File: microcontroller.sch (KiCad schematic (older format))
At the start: 8 parts

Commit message: Basic schematic with temparature and humidity sensor.
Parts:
- removed U?: STM32F072C8T, LQFP48, symbol STM32F072C8T
- added C?: 100n, symbol C
- added C?: C, symbol C
- added P?: DEBUG_UART, symbol CONN_01X03
- added R? (x2): 3k3, symbol R
- added SW?: SW_PUSH, symbol SW_PUSH
- added U?: STM32F072RB, symbol STM32F072RB
- added U?: HDC1080, symbol HDC1080
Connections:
- net labels added: CAN_RX, CAN_STANDBY, CAN_TX, GPIO_PB4_OUT, I2C1_SCL, I2C1_SDA, UART_RX, UART_TX
- wire segments 28 -> 63
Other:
- moved on the sheet: C?, X?

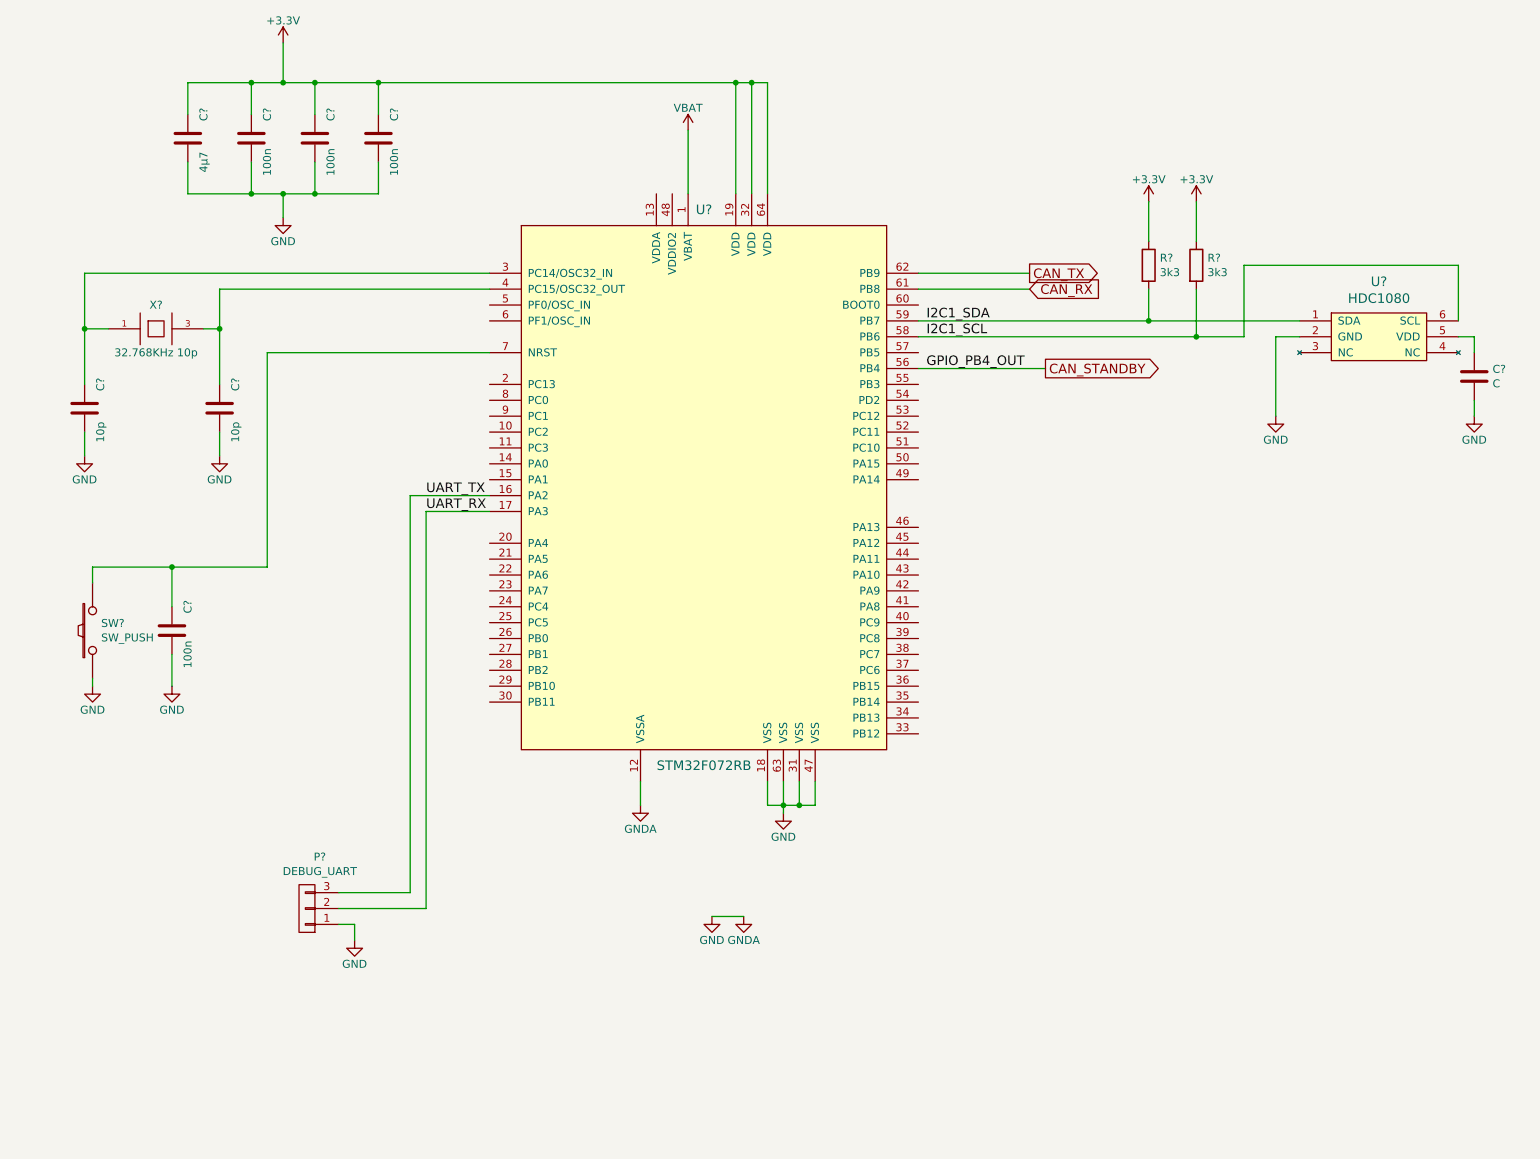
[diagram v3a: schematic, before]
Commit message: Add flash and debug connector.
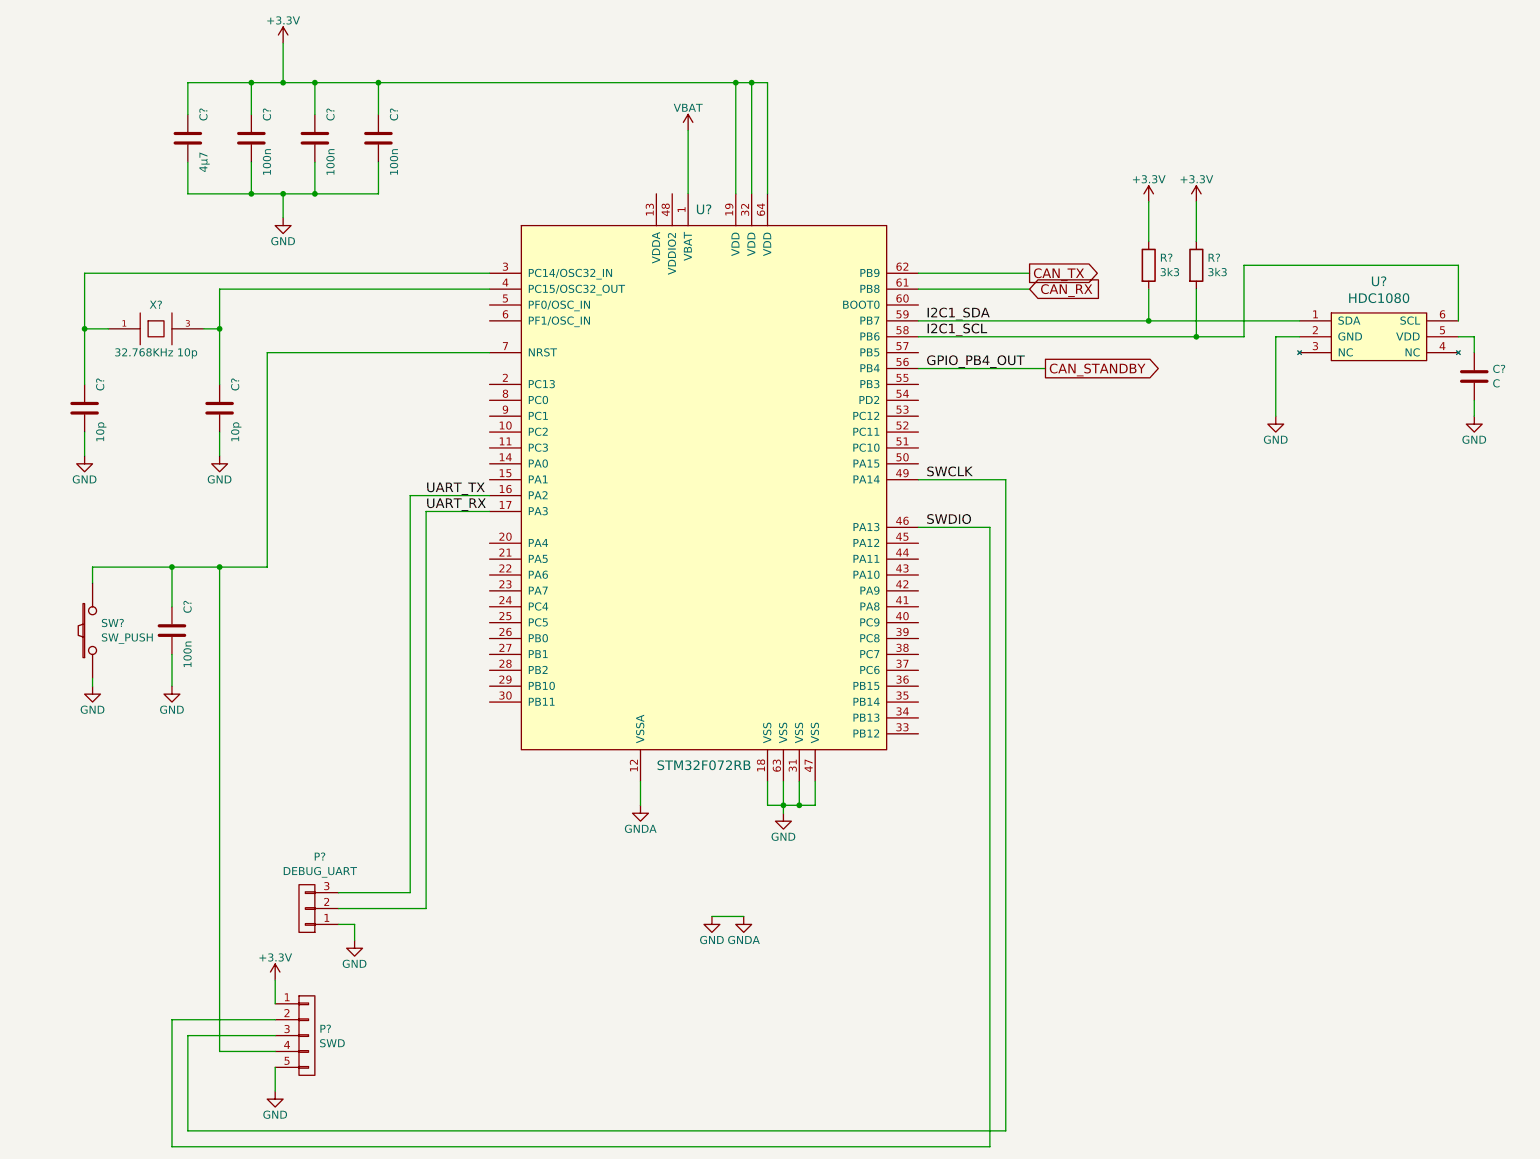
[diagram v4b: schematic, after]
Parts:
- added P?: SWD, symbol CONN_01X05
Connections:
- net +3V3: now also P?.1 (P1)
- net GND: now also P?.5 (P5)
- net SWDIO: now reaches U?.46 (PA13)
- net SWDIO: now also P?.2 (P2)
- net SWCLK: now reaches U?.49 (PA14)
- net SWCLK: now also P?.3 (P3)
- net at C?.1, SW?.2, U?.7 (NRST): now also P?.4 (P4)
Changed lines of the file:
@@
 Wire Wire Line
 	6200 2800 7000 2800
+$Comp
+L CONN_01X05 P?
+U 1 1 57AF82F1
+P 2350 7000
+F 0 "P?" H 2428 7041 50  0000 L CNN
+F 1 "SWD" H 2428 6950 50  0000 L CNN
+F 2 "" H 2350 7000 50  0000 C CNN
+F 3 "" H 2350 7000 50  0000 C CNN
+	1    2350 7000
+	1    0    0    -1
+$EndComp
+$Comp
+L GND #PWR?
+U 1 1 57AF8433
+P 2150 7350
+F 0 "#PWR?" H 2150 7100 50  0001 C CNN
+F 1 "GND" H 2150 7200 50  0000 C CNN
+F 2 "" H 2150 7350 60  0000 C CNN
+F 3 "" H 2150 7350 60  0000 C CNN
+	1    2150 7350
+	1    0    0    -1
+$EndComp
+Wire Wire Line
+	2150 7350 2150 7200
+$Comp
+L +3.3V #PWR?
+U 1 1 57AF8559
+P 2150 6650
+F 0 "#PWR?" H 2150 6500 50  0001 C CNN
+F 1 "+3.3V" H 2150 6790 50  0000 C CNN
+F 2 "" H 2150 6650 60  0000 C CNN
+F 3 "" H 2150 6650 60  0000 C CNN
+	1    2150 6650
+	1    0    0    -1
+$EndComp
+Wire Wire Line
+	2150 6800 2150 6650
+Wire Wire Line
+	2150 6900 1500 6900
+Text Label 6250 3800 0    60   ~ 0
+SWDIO
+Wire Wire Line
+	6200 3500 6750 3500
+Wire Wire Line
+	6750 3500 6750 7600
+Wire Wire Line
+	1600 7000 2150 7000
+Text Label 6250 3500 0    60   ~ 0
+SWCLK
+Wire Wire Line
+	1600 7000 1600 7600
+Wire Wire Line
+	1600 7600 6750 7600
+Wire Wire Line
+	6200 3800 6650 3800
+Wire Wire Line
+	6650 3800 6650 7700
+Wire Wire Line
+	6650 7700 1500 7700
+Wire Wire Line
+	1500 7700 1500 6900
+Wire Wire Line
+	2150 7100 1800 7100
+Wire Wire Line
+	1800 7100 1800 4050
+Connection ~ 1800 4050
 $EndSCHEMATC

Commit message: .
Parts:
- added Q?: Q_NMOS_DGS, symbol Q_NMOS_DGS
- C19, C20, C21: renamed from C?; footprint (none) -> Capacitors_SMD:C_0603_HandSoldering
- R15, R16: renamed from R?; footprint (none) -> Resistors_SMD:R_0603_HandSoldering
- U3: renamed from U?; footprint (none) -> can-node:LQFP64_STM
- gave numbers to parts that had none: 10
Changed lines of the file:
@@
 $EndDescr
 $Comp
-L +3.3V #PWR029
+L +3.3V #PWR028
 U 1 1 562B6336
 P 2200 750
-F 0 "#PWR029" H 2200 600 50  0001 C CNN
+F 0 "#PWR028" H 2200 600 50  0001 C CNN
 F 1 "+3.3V" H 2200 890 50  0000 C CNN
 F 2 "" H 2200 750 60  0000 C CNN
@@
 $EndComp
 $Comp
-L QUARTZCMS4 X?
+L QUARTZCMS4 X1
 U 1 1 562B633C
 P 1400 2550
-F 0 "X?" H 1400 2700 50  0000 C CNN
+F 0 "X1" H 1400 2700 50  0000 C CNN
 F 1 "32.768KHz 10p" H 1400 2400 50  0000 C CNN
-F 2 "" H 1400 2550 60  0000 C CNN
+F 2 "" H 1400 2550 60  0001 C CNN
 F 3 "" H 1400 2550 60  0000 C CNN
 	1    1400 2550
@@
 $EndComp
 $Comp
-L C C?
+L C C18
 U 1 1 562B6351
 P 1800 3050
-F 0 "C?" V 1900 3200 50  0000 C CNN
+F 0 "C18" V 1900 3200 50  0000 C CNN
 F 1 "10p" V 1900 2900 50  0000 C CNN
-F 2 "" H 1800 3050 60  0000 C CNN
+F 2 "" H 1800 3050 60  0001 C CNN
 F 3 "" H 1800 3050 60  0000 C CNN
 	1    1800 3050
@@
 $EndComp
 $Comp
-L C C?
+L C C15
 U 1 1 562B6358
 P 950 3050
-F 0 "C?" V 1050 3200 50  0000 C CNN
+F 0 "C15" V 1050 3200 50  0000 C CNN
 F 1 "10p" V 1050 2900 50  0000 C CNN
-F 2 "" H 950 3050 60  0000 C CNN
+F 2 "" H 950 3050 60  0001 C CNN
 F 3 "" H 950 3050 60  0000 C CNN
 	1    950  3050
@@
 $EndComp
 $Comp
-L GND #PWR030
+L GND #PWR029
 U 1 1 562B635F
 P 950 3350
-F 0 "#PWR030" H 950 3100 50  0001 C CNN
+F 0 "#PWR029" H 950 3100 50  0001 C CNN
 F 1 "GND" H 950 3200 50  0000 C CNN
 F 2 "" H 950 3350 60  0000 C CNN
@@
 $EndComp
 $Comp
-L GND #PWR031
+L GND #PWR030
 U 1 1 562B6365
 P 1800 3350
-F 0 "#PWR031" H 1800 3100 50  0001 C CNN
+F 0 "#PWR030" H 1800 3100 50  0001 C CNN
 F 1 "GND" H 1800 3200 50  0000 C CNN
 F 2 "" H 1800 3350 60  0000 C CNN
@@
 $EndComp
 $Comp
-L GND #PWR032
+L GND #PWR031
 U 1 1 562B636B
 P 5350 5600
-F 0 "#PWR032" H 5350 5350 50  0001 C CNN
+F 0 "#PWR031" H 5350 5350 50  0001 C CNN
 F 1 "GND" H 5350 5450 50  0000 C CNN
 F 2 "" H 5350 5600 60  0000 C CNN
@@
 $EndComp
 $Comp
-L GND #PWR033
+L GND #PWR032
 U 1 1 562B6371
 P 4900 6250
-F 0 "#PWR033" H 4900 6000 50  0001 C CNN
+F 0 "#PWR032" H 4900 6000 50  0001 C CNN
 F 1 "GND" H 4900 6100 50  0000 C CNN
 F 2 "" H 4900 6250 60  0000 C CNN
@@
 $EndComp
 $Comp
-L GNDA #PWR034
+L GNDA #PWR033
 U 1 1 562B6377
 P 4450 5550
-F 0 "#PWR034" H 4450 5300 50  0001 C CNN
+F 0 "#PWR033" H 4450 5300 50  0001 C CNN
 F 1 "GNDA" H 4450 5400 50  0000 C CNN
 F 2 "" H 4450 5550 60  0000 C CNN
@@
 $EndComp
 $Comp
-L GNDA #PWR035
+L GNDA #PWR034
 U 1 1 562B637D
 P 5100 6250
-F 0 "#PWR035" H 5100 6000 50  0001 C CNN
+F 0 "#PWR034" H 5100 6000 50  0001 C CNN
 F 1 "GNDA" H 5100 6100 50  0000 C CNN
 F 2 "" H 5100 6250 60  0000 C CNN
@@
 $EndComp
 $Comp
-L C C?
+L C C21
 U 1 1 562B6383
 P 2800 1350
-F 0 "C?" V 2900 1500 50  0000 C CNN
+F 0 "C21" V 2900 1500 50  0000 C CNN
 F 1 "100n" V 2900 1200 50  0000 C CNN
-F 2 "" H 2800 1350 60  0000 C CNN
+F 2 "Capacitors_SMD:C_0603_HandSoldering" H 2800 1350 60  0001 C CNN
 F 3 "" H 2800 1350 60  0000 C CNN
 	1    2800 1350
@@
 $EndComp
 $Comp
-L C C?
+L C C20
 U 1 1 562B638A
 P 2400 1350
-F 0 "C?" V 2500 1500 50  0000 C CNN
+F 0 "C20" V 2500 1500 50  0000 C CNN
 F 1 "100n" V 2500 1200 50  0000 C CNN
-F 2 "" H 2400 1350 60  0000 C CNN
+F 2 "Capacitors_SMD:C_0603_HandSoldering" H 2400 1350 60  0001 C CNN
 F 3 "" H 2400 1350 60  0000 C CNN
 	1    2400 1350
@@
 $EndComp
 $Comp
-L C C?
+L C C19
 U 1 1 562B6391
 P 2000 1350
-F 0 "C?" V 2100 1500 50  0000 C CNN
+F 0 "C19" V 2100 1500 50  0000 C CNN
 F 1 "100n" V 2100 1200 50  0000 C CNN
-F 2 "" H 2000 1350 60  0000 C CNN
+F 2 "Capacitors_SMD:C_0603_HandSoldering" H 2000 1350 60  0001 C CNN
 F 3 "" H 2000 1350 60  0000 C CNN
 	1    2000 1350
@@
 $EndComp
 $Comp
-L C C?
+L C C17
 U 1 1 562B6398
 P 1600 1350
-F 0 "C?" V 1700 1500 50  0000 C CNN
+F 0 "C17" V 1700 1500 50  0000 C CNN
 F 1 "4µ7" V 1700 1200 50  0000 C CNN
-F 2 "" H 1600 1350 60  0000 C CNN
+F 2 "" H 1600 1350 60  0001 C CNN
 F 3 "" H 1600 1350 60  0000 C CNN
 	1    1600 1350
@@
 Connection ~ 2000 1700
 $Comp
-L GND #PWR036
+L GND #PWR035
 U 1 1 562B63C4
 P 2200 1850
-F 0 "#PWR036" H 2200 1600 50  0001 C CNN
+F 0 "#PWR035" H 2200 1600 50  0001 C CNN
 F 1 "GND" H 2200 1700 50  0000 C CNN
 F 2 "" H 2200 1850 60  0000 C CNN
@@
 Connection ~ 2200 1000
 $Comp
-L VBAT #PWR037
+L VBAT #PWR036
 U 1 1 562C42F9
 P 4750 1300
-F 0 "#PWR037" H 4750 1150 50  0001 C CNN
+F 0 "#PWR036" H 4750 1150 50  0001 C CNN
 F 1 "VBAT" H 4750 1440 50  0000 C CNN
 F 2 "" H 4750 1300 60  0000 C CNN
@@
 	4750 1700 4750 1300
 $Comp
-L STM32F072RB U?
+L STM32F072RB U3
 U 1 1 57A64432
 P 4850 3550
-F 0 "U?" H 4850 5300 60  0000 C CNN
+F 0 "U3" H 4850 5300 60  0000 C CNN
 F 1 "STM32F072RB" H 4850 1800 60  0000 C CNN
-F 2 "" H 4850 3550 60  0000 C CNN
+F 2 "can-node:LQFP64_STM" H 4850 3550 60  0001 C CNN
 F 3 "" H 4850 3550 60  0000 C CNN
 	1    4850 3550
@@
 Connection ~ 5050 1000
 $Comp
-L C C?
+L C C16
 U 1 1 57ADEBC4
 P 1500 4450
-F 0 "C?" V 1600 4600 50  0000 C CNN
+F 0 "C16" V 1600 4600 50  0000 C CNN
 F 1 "100n" V 1600 4300 50  0000 C CNN
-F 2 "" H 1500 4450 60  0000 C CNN
+F 2 "" H 1500 4450 60  0001 C CNN
 F 3 "" H 1500 4450 60  0000 C CNN
 	1    1500 4450
@@
 $EndComp
 $Comp
-L SW_PUSH SW?
+L SW_PUSH SW1
 U 1 1 57ADEE8E
 P 1000 4450
-F 0 "SW?" V 1046 4396 50  0000 R CNN
+F 0 "SW1" V 1046 4396 50  0000 R CNN
 F 1 "SW_PUSH" V 955 4396 50  0000 R CNN
-F 2 "" H 1000 4450 50  0000 C CNN
+F 2 "" H 1000 4450 50  0001 C CNN
 F 3 "" H 1000 4450 50  0000 C CNN
 	1    1000 4450
@@
 $EndComp
 $Comp
-L GND #PWR?
+L GND #PWR037
 U 1 1 57ADF092
 P 1500 4800
-F 0 "#PWR?" H 1500 4550 50  0001 C CNN
+F 0 "#PWR037" H 1500 4550 50  0001 C CNN
 F 1 "GND" H 1500 4650 50  0000 C CNN
 F 2 "" H 1500 4800 60  0000 C CNN
@@
 	1500 4600 1500 4800
 $Comp
-L GND #PWR?
+L GND #PWR038
 U 1 1 57ADF227
 P 1000 4800
-F 0 "#PWR?" H 1000 4550 50  0001 C CNN
+F 0 "#PWR038" H 1000 4550 50  0001 C CNN
 F 1 "GND" H 1000 4650 50  0000 C CNN
 F 2 "" H 1000 4800 60  0000 C CNN
@@
 I2C1_SDA
 $Comp
-L CONN_01X03 P?
+L CONN_01X03 P1
 U 1 1 57AF6015
 P 2350 6200
-F 0 "P?" H 2269 5875 50  0000 C CNN
+F 0 "P1" H 2269 5875 50  0000 C CNN
 F 1 "DEBUG_UART" H 2269 5966 50  0000 C CNN
-F 2 "" H 2350 6200 50  0000 C CNN
+F 2 "" H 2350 6200 50  0001 C CNN
 F 3 "" H 2350 6200 50  0000 C CNN
 	1    2350 6200
@@
 	3100 3700 3500 3700
 $Comp
-L GND #PWR?
+L GND #PWR039
 U 1 1 57AF6194
 P 2650 6400
-F 0 "#PWR?" H 2650 6150 50  0001 C CNN
+F 0 "#PWR039" H 2650 6150 50  0001 C CNN
 F 1 "GND" H 2650 6250 50  0000 C CNN
 F 2 "" H 2650 6400 60  0000 C CNN
@@
 UART_RX
 $Comp
-L HDC1080 U?
+L HDC1080 U4
 U 1 1 57AF6711
 P 9100 2600
-F 0 "U?" H 9100 2947 60  0000 C CNN
+F 0 "U4" H 9100 2947 60  0000 C CNN
 F 1 "HDC1080" H 9100 2841 60  0000 C CNN
-F 2 "" H 9100 2600 60  0000 C CNN
+F 2 "" H 9100 2600 60  0001 C CNN
 F 3 "" H 9100 2600 60  0000 C CNN
 	1    9100 2600
@@
 	9600 2150 9600 2500
 $Comp
-L +3.3V #PWR?
+L +3.3V #PWR040
 U 1 1 57AF69E7
 P 7650 1750
-F 0 "#PWR?" H 7650 1600 50  0001 C CNN
+F 0 "#PWR040" H 7650 1600 50  0001 C CNN
 F 1 "+3.3V" H 7650 1890 50  0000 C CNN
 F 2 "" H 7650 1750 60  0000 C CNN
@@
 $EndComp
 $Comp
-L +3.3V #PWR?
+L +3.3V #PWR041
 U 1 1 57AF6AA6
 P 7950 1750
-F 0 "#PWR?" H 7950 1600 50  0001 C CNN
+F 0 "#PWR041" H 7950 1600 50  0001 C CNN
 F 1 "+3.3V" H 7950 1890 50  0000 C CNN
 F 2 "" H 7950 1750 60  0000 C CNN
@@
 $EndComp
 $Comp
-L R R?
+L R R15
 U 1 1 57AF6ACB
 P 7650 2150
-F 0 "R?" H 7720 2196 50  0000 L CNN
+F 0 "R15" H 7720 2196 50  0000 L CNN
 F 1 "3k3" H 7720 2105 50  0000 L CNN
-F 2 "" V 7580 2150 50  0000 C CNN
+F 2 "Resistors_SMD:R_0603_HandSoldering" V 7580 2150 50  0001 C CNN
 F 3 "" H 7650 2150 50  0000 C CNN
 	1    7650 2150
@@
 $EndComp
 $Comp
-L R R?
+L R R16
 U 1 1 57AF6B19
 P 7950 2150
-F 0 "R?" H 8020 2196 50  0000 L CNN
+F 0 "R16" H 8020 2196 50  0000 L CNN
 F 1 "3k3" H 8020 2105 50  0000 L CNN
-F 2 "" V 7880 2150 50  0000 C CNN
+F 2 "Resistors_SMD:R_0603_HandSoldering" V 7880 2150 50  0001 C CNN
 F 3 "" H 7950 2150 50  0000 C CNN
 	1    7950 2150
@@
 	7950 2000 7950 1750
 $Comp
-L C C?
+L C C22
 U 1 1 57AF6E3D
 P 9700 2850
-F 0 "C?" H 9815 2896 50  0000 L CNN
+F 0 "C22" H 9815 2896 50  0000 L CNN
 F 1 "C" H 9815 2805 50  0000 L CNN
-F 2 "" H 9738 2700 50  0000 C CNN
+F 2 "" H 9738 2700 50  0001 C CNN
 F 3 "" H 9700 2850 50  0000 C CNN
 	1    9700 2850
@@
 $EndComp
 $Comp
-L GND #PWR?
+L GND #PWR042
 U 1 1 57AF7025
 P 9700 3100
-F 0 "#PWR?" H 9700 2850 50  0001 C CNN
+F 0 "#PWR042" H 9700 2850 50  0001 C CNN
 F 1 "GND" H 9700 2950 50  0000 C CNN
 F 2 "" H 9700 3100 60  0000 C CNN
@@
 	9700 2600 9600 2600
 $Comp
-L GND #PWR?
+L GND #PWR043
 U 1 1 57AF718A
 P 8450 3100
-F 0 "#PWR?" H 8450 2850 50  0001 C CNN
+F 0 "#PWR043" H 8450 2850 50  0001 C CNN
 F 1 "GND" H 8450 2950 50  0000 C CNN
 F 2 "" H 8450 3100 60  0000 C CNN
@@
 	6200 2800 7000 2800
 $Comp
-L CONN_01X05 P?
+L CONN_01X05 P2
 U 1 1 57AF82F1
 P 2350 7000
-F 0 "P?" H 2428 7041 50  0000 L CNN
+F 0 "P2" H 2428 7041 50  0000 L CNN
 F 1 "SWD" H 2428 6950 50  0000 L CNN
-F 2 "" H 2350 7000 50  0000 C CNN
+F 2 "" H 2350 7000 50  0001 C CNN
 F 3 "" H 2350 7000 50  0000 C CNN
 	1    2350 7000
@@
 $EndComp
 $Comp
-L GND #PWR?
+L GND #PWR044
 U 1 1 57AF8433
 P 2150 7350
-F 0 "#PWR?" H 2150 7100 50  0001 C CNN
+F 0 "#PWR044" H 2150 7100 50  0001 C CNN
 F 1 "GND" H 2150 7200 50  0000 C CNN
 F 2 "" H 2150 7350 60  0000 C CNN
@@
 	2150 7350 2150 7200
 $Comp
-L +3.3V #PWR?
+L +3.3V #PWR045
 U 1 1 57AF8559
 P 2150 6650
-F 0 "#PWR?" H 2150 6500 50  0001 C CNN
+F 0 "#PWR045" H 2150 6500 50  0001 C CNN
 F 1 "+3.3V" H 2150 6790 50  0000 C CNN
 F 2 "" H 2150 6650 60  0000 C CNN
@@
 	1800 7100 1800 4050
 Connection ~ 1800 4050
+$Comp
+L Q_NMOS_DGS Q?
+U 1 1 57AFA1F2
+P 9000 4700
+F 0 "Q?" H 9191 4746 50  0000 L CNN
+F 1 "Q_NMOS_DGS" H 9191 4655 50  0000 L CNN
+F 2 "" H 9200 4800 50  0000 C CNN
+F 3 "" H 9000 4700 50  0000 C CNN
+	1    9000 4700
+	1    0    0    -1
+$EndComp
 $EndSCHEMATC

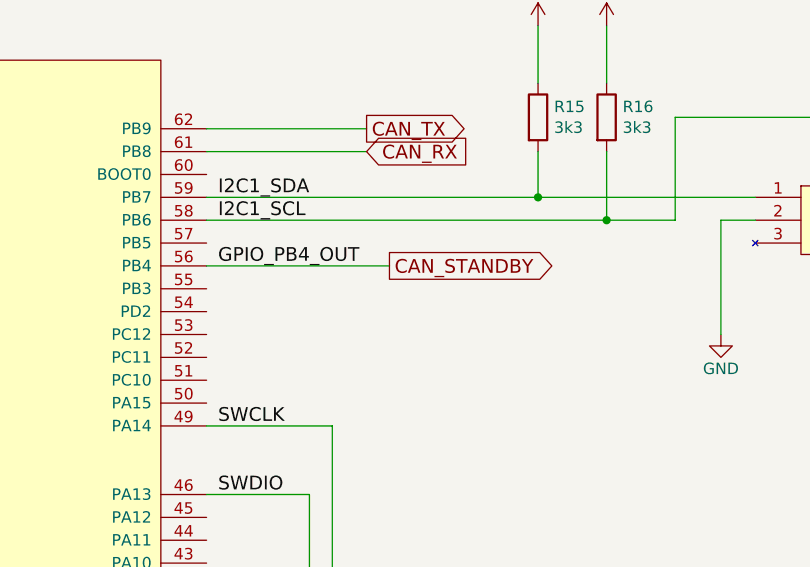
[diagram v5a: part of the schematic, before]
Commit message: Use TI TCAN334 3.3V CAN transceiver.
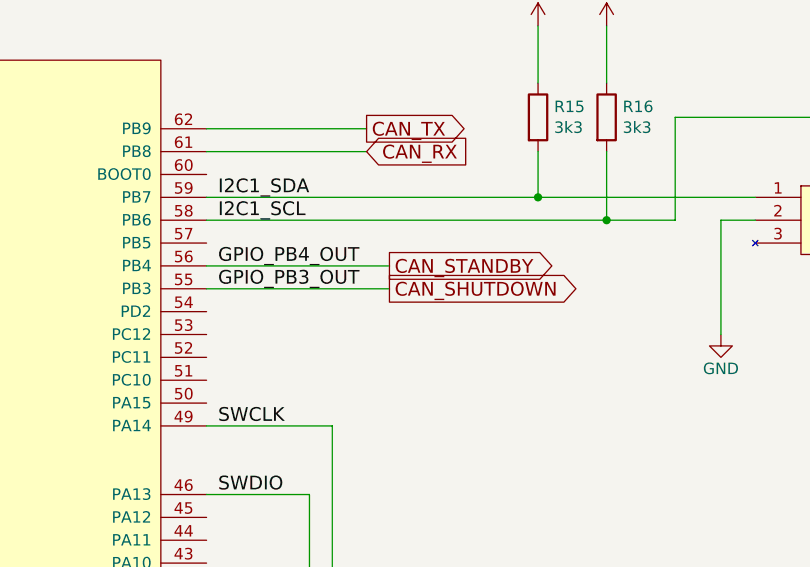
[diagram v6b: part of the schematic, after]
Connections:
- net CAN_SHUTDOWN: now reaches U3.55 (PB3)
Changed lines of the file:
@@
 	1    0    0    -1
 $EndComp
+Text GLabel 7000 2900 2    60   Output ~ 0
+CAN_SHUTDOWN
+Wire Wire Line
+	7000 2900 6200 2900
+Text Label 6250 2900 0    60   ~ 0
+GPIO_PB3_OUT
 $EndSCHEMATC
